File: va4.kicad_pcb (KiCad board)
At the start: 2 copper layers, 95.8 x 73.1 mm, 17 parts, among them J1 LED, J2 MJ-4PP-9, SW1 RESET_SWITCH, SW2 SW_PUSH, SW3 SW_PUSH, SW4 SW_PUSH, SW5 SW_PUSH, SW6 Rotary_Encoder_Switch, U1 ProMicro

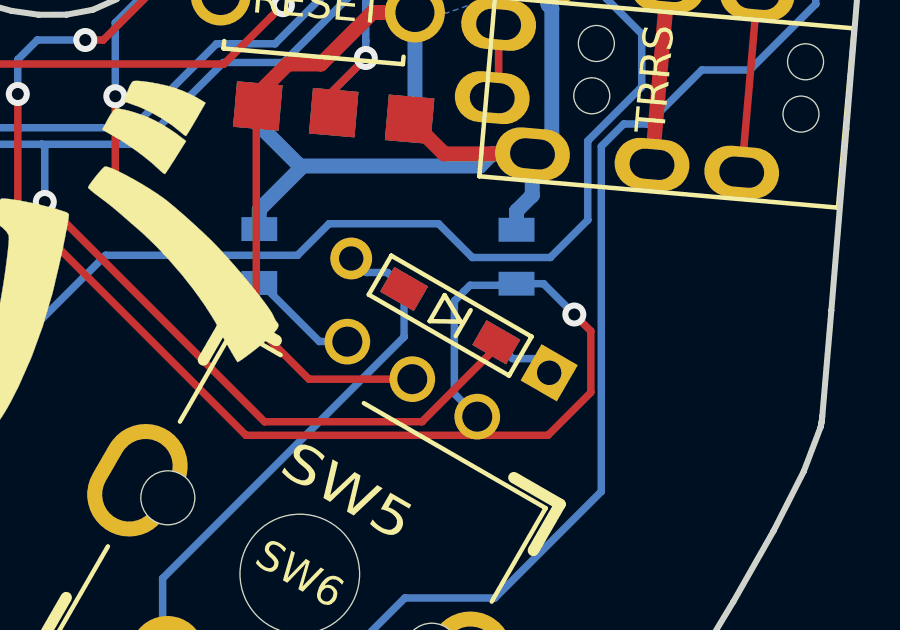
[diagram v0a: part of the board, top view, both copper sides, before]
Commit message: Fix D4 front pad
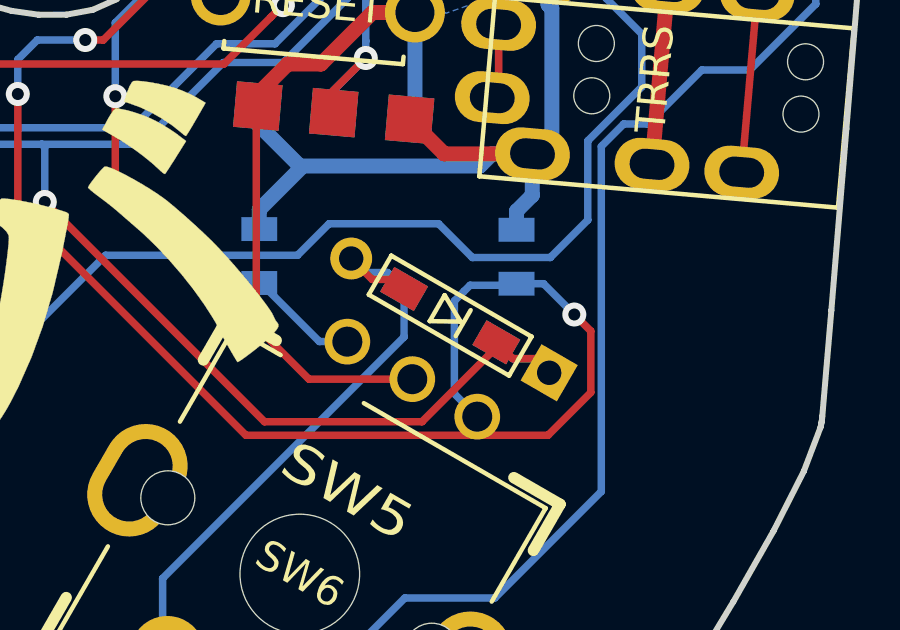
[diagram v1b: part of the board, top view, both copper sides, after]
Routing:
- net row0: track 144.9 -> 147.1 mm
- net Enc1Row0: track 20.3 -> 22.2 mm
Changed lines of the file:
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@@
     (thickness 1.6)
     (drawings 157)
-    (tracks 538)
+    (tracks 543)
     (zones 0)
     (modules 17)
@@
   (segment (start 122.75 77.075) (end 122.75 77.25) (width 0.25) (layer F.Cu) (net 17))
   (segment (start 122.75 77.25) (end 120.275 79.725) (width 0.25) (layer F.Cu) (net 17))
+  (segment (start 123.296543 77.621543) (end 124.071543 77.621543) (width 0.25) (layer F.Cu) (net 17))
+  (segment (start 122.75 77.075) (end 123.296543 77.621543) (width 0.25) (layer F.Cu) (net 17))
+  (segment (start 124.071543 77.621543) (end 124.5 78.05) (width 0.25) (layer F.Cu) (net 17))
   (segment (start 131.532476 46.096065) (end 132.104598 46.096065) (width 0.25) (layer B.Cu) (net 18))
   (segment (start 118.480881 45.919119) (end 121 43.4) (width 0.25) (layer B.Cu) (net 18))
@@
   (segment (start 119.67561 75.3) (end 119.12561 74.75) (width 0.25) (layer B.Cu) (net 25))
   (segment (start 119.12561 74.75) (end 118.425 74.75) (width 0.25) (layer B.Cu) (net 25))
+  (segment (start 118.611747 74.980999) (end 119.430999 74.980999) (width 0.25) (layer F.Cu) (net 25))
+  (segment (start 117.913248 74.2825) (end 118.611747 74.980999) (width 0.25) (layer F.Cu) (net 25))
   (segment (start 130.776344 61.278072) (end 131.853974 61.278072) (width 0.25) (layer B.Cu) (net 26))
   (segment (start 130.078072 61.278072) (end 130.776344 61.278072) (width 0.25) (layer B.Cu) (net 26))
